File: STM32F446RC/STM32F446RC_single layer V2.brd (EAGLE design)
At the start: 74.9 x 25.4 mm, 75 parts, among them IC1 STM32F446RCT6

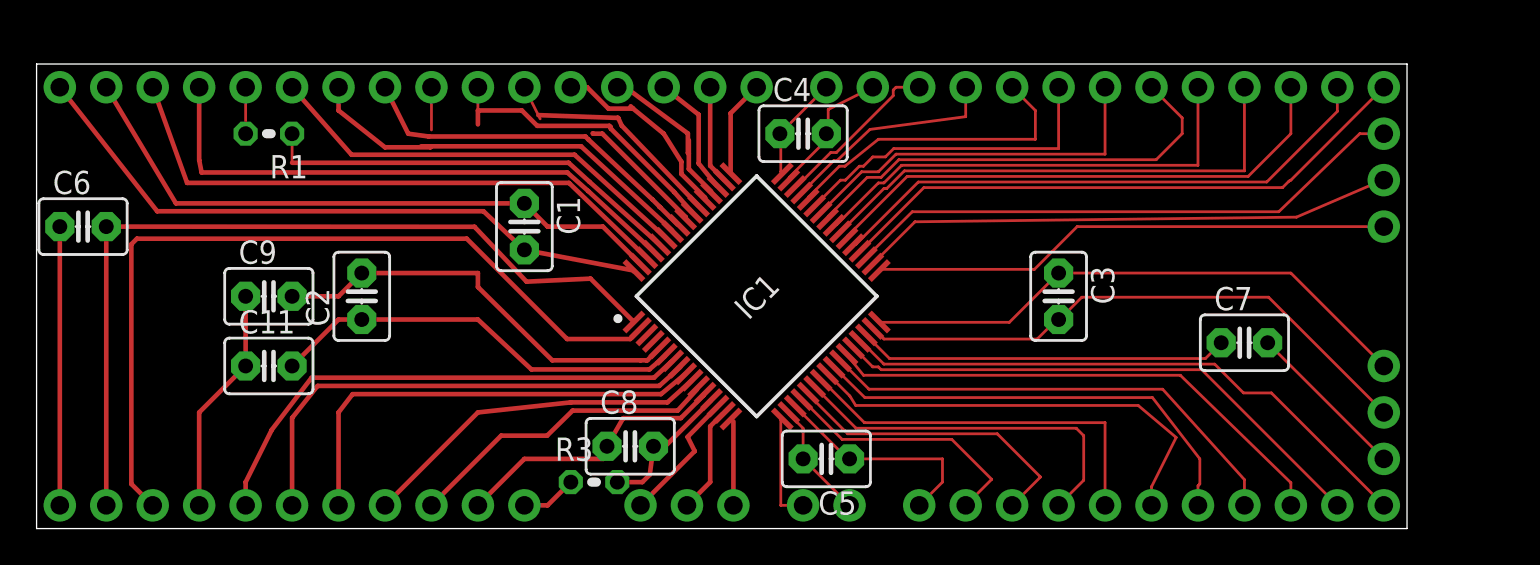
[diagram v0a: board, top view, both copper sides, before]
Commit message: added double layer
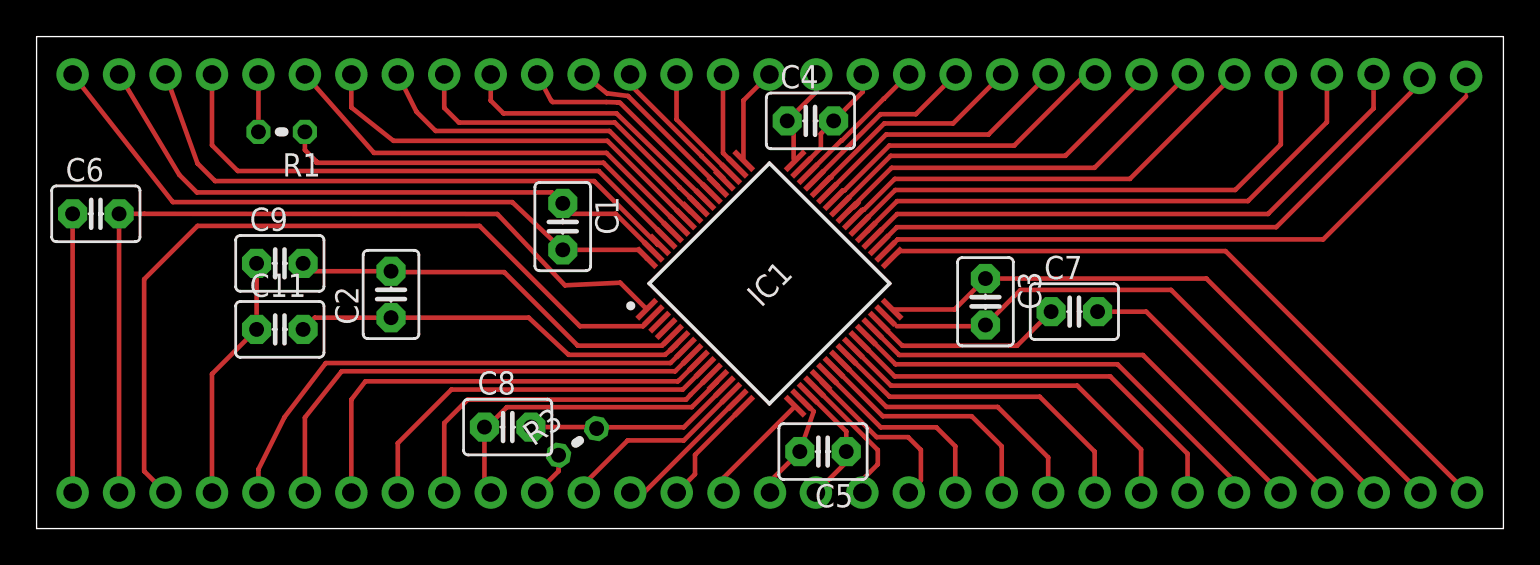
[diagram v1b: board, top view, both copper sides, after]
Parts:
- C1, C3, C4, C5, C6: value 100n+1u -> 100n
- C11, C2, C9: value 20p -> 22p
- R3: value (none) -> 47
- moved JP18 15.2 mm to (78.2, 1.97)
- moved C7 9.45 mm to (56.7, 11.9)
- moved JP13 7.22 mm to (78.2, 24.7)
- moved JP51 7.20 mm to (75.7, 1.97)
- moved C8 6.78 mm to (25.8, 5.55)
- moved JP16 5.69 mm to (65.5, 1.97)
- moved JP19 5.69 mm to (47.7, 1.97)
- moved JP22 5.69 mm to (60.4, 1.97)
- moved JP9 5.69 mm to (50.2, 1.97)
- moved JP11 5.69 mm to (52.8, 1.97)
- moved JP12 5.69 mm to (55.3, 1.97)
- moved JP17 5.69 mm to (62.9, 1.97)
- moved JP21 5.69 mm to (45.1, 1.97)
- moved JP23 5.69 mm to (57.9, 1.97)
- moved JP48 5.69 mm to (42.6, 1.97)
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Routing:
- net N$66: track 20.3 -> 10.7 mm
- net N$11: track 24.5 -> 15.5 mm
- net N$18: track 20.2 -> 11.2 mm
- net N$43: track 9.61 -> 18.1 mm
- net N$21: track 28.6 -> 37.0 mm
- net N$54: track 9.09 -> 16.8 mm
- net N$17: track 21.0 -> 13.6 mm
- net N$22: track 29.3 -> 36.6 mm
- net N$19: track 16.8 -> 9.67 mm
- net N$12: track 24.9 -> 18.0 mm
- net N$52: track 14.2 -> 7.65 mm
- net N$16: track 32.3 -> 26.1 mm
- net N$13: track 26.3 -> 20.4 mm
- net N$14: track 28.4 -> 22.7 mm
- net N$15: track 30.0 -> 24.2 mm
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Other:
- board size 74.9 x 25.4 mm -> 80.2 x 26.9 mm
